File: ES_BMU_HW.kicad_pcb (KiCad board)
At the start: 2 copper layers, 100 x 100 mm, 105 parts, among them IC1 ADBMS6821CCSZ, J5 Conn_02x03_Top_Bottom, K1 FINDER-30.22, Q1 Si2366DS, Q2 Si2366DS, Q3 Si2366DS, Q4 2N7002, Q5 SQ2337CES, Q6 2N7002, SW3 SW_Nidec_CAS-120A1, T1 74941301, U1 TPS542025, U12 LM393, U13 74HC32, U15 SN65HVD235, U17 74AUP1G02, U18 74AUP1G08, U3 TLV1702, U4 TLV1702, U5 TLV1702, U6 STM32G474CETx, U7 TLV777, U8 TLV1704, U9 74HC04, Y1 16 MHz

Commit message: Canvi de microcontrolador Control dels relés de potència actualitzat Leds afegits per a visualitzar l'estat del fusible
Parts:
- removed C18, C19: 22p, Capacitor_SMD:C_1206_3216Metric
- removed K1: FINDER-30.22, Relay_THT:Relay_DPDT_Finder_30.22
- removed R1, R12, R14, R28, R7: 10K, Resistor_SMD:R_1206_3216Metric
- removed R13, R17, R22, R29, R5: 100K, Resistor_SMD:R_1206_3216Metric
- removed TP1, TP2, TP3, TP4: TestPoint, TestPoint:TestPoint_Pad_D1.0mm
- removed U13: 74HC32, Package_SO:TSSOP-14_4.4x5mm_P0.65mm
- removed U17: 74AUP1G02, Package_TO_SOT_SMD:Texas_R-PDSO-G5_DCK-5
- removed U18: 74AUP1G08, Package_TO_SOT_SMD:Texas_R-PDSO-G5_DCK-5
- removed U3, U4: TLV1702, Package_SO:VSSOP-8_3x3mm_P0.65mm
- removed U6: STM32G474CETx, Package_QFP:LQFP-48_7x7mm_P0.5mm
- removed U8: TLV1704, Package_SO:TSSOP-14_4.4x5mm_P0.65mm
- removed Y1: 16 MHz, Crystal_SMD_Wurth:Y_Wurth_WE-XTAL_Quartz-CFPX-180
- added C12: 10u, Capacitor_SMD:C_0603_1608Metric, F.Cu at (42.1, 61.0)
- added C16: 22p, Capacitor_SMD:C_1206_3216Metric, F.Cu at (66.2, 91.0)
- added C26: 22p, Capacitor_SMD:C_1206_3216Metric, F.Cu at (66.2, 94.4)
- added C27: 100n, Capacitor_SMD:C_0603_1608Metric, F.Cu at (42.1, 71.0)
- added D10: SMAJ30A, Diode_SMD:D_SMA, F.Cu at (23.1, 80.2)
- added D11: SMBJ3V3, Diode_SMD:D_SMB, F.Cu at (23.3, 89.8)
- added D12: SMBJ3V3, Diode_SMD:D_SMB, F.Cu at (23.3, 95.3)
- added D13: SMAJ30A, Diode_SMD:D_SMA, F.Cu at (23.1, 84.7)
- added D14: AR1FJ, Diode_SMD:D_SMF, F.Cu at (44.1, 89.1)
- added D16: SMAJ30A, Diode_SMD:D_SMA, F.Cu at (31.2, 62.0)
- added D17: SMAJ30A, Diode_SMD:D_SMA, F.Cu at (31.2, 66.5)
- added D19: SMAJ30A, Diode_SMD:D_SMA, F.Cu at (31.2, 71.1)
- added D2: SMAJ30A, Diode_SMD:D_SMA, F.Cu at (23.1, 62.0)
- added D20: AR1FJ, Diode_SMD:D_SMF, F.Cu at (44.1, 92.4)
- added D21: SMAJ30A, Diode_SMD:D_SMA, F.Cu at (31.2, 75.6)
- added D22: AR1FJ, Diode_SMD:D_SMF, F.Cu at (44.1, 95.8)
- added D23: SMAJ30A, Diode_SMD:D_SMA, F.Cu at (53.0, 66.5)
- added D24: D_Schottky, Diode_SMD:D_SMA, F.Cu at (53.0, 71.1)
- added D25: SMAJ30A, Diode_SMD:D_SMA, F.Cu at (53.0, 75.6)
- added D26: D_Schottky, Diode_SMD:D_SMA, F.Cu at (53.0, 80.2)
- added D27: SMAJ30A, Diode_SMD:D_SMA, F.Cu at (53.0, 84.7)
- added D28: SMAJ30A, Diode_SMD:D_SMA, F.Cu at (31.2, 80.2)
- added D3: SMAJ30A, Diode_SMD:D_SMA, F.Cu at (23.1, 66.5)
- added F2: Fuse, Fuse:Fuse_1206_3216Metric_Pad1.42x1.75mm_HandSolder, F.Cu at (38.2, 89.1)
- added F5: Fuse, Fuse:Fuse_1206_3216Metric_Pad1.42x1.75mm_HandSolder, F.Cu at (38.2, 92.4)
- added F6: Fuse, Fuse:Fuse_1206_3216Metric_Pad1.42x1.75mm_HandSolder, F.Cu at (38.2, 95.7)
- added Q7: SQ2362CES, Package_TO_SOT_SMD:SOT-23, F.Cu at (37.7, 71.4)
- added Q8: SQ2362CES, Package_TO_SOT_SMD:SOT-23, F.Cu at (37.7, 76.0)
- added R52: 100k, Resistor_SMD:R_0201_0603Metric_Pad0.64x0.40mm_HandSolder, F.Cu at (64.1, 77.9)
- added R53: 100k, Resistor_SMD:R_0201_0603Metric_Pad0.64x0.40mm_HandSolder, F.Cu at (64.1, 79.6)
- added U10: STM32G431RBTx, Package_QFP:LQFP-64_10x10mm_P0.5mm, F.Cu at (56.2, 96.6)
- added U11: LM393, Package_SO:TSSOP-8_4.4x3mm_P0.65mm, F.Cu at (61.4, 66.6)
- added U2: LM393, Package_SO:TSSOP-8_4.4x3mm_P0.65mm, F.Cu at (39.6, 80.5)
- added Y2: 16 MHz, Crystal_SMD_Wurth:Y_Wurth_WE-XTAL_Quartz-CFPX-180, F.Cu at (65.7, 98.7)
- C10, C15: value 15pF -> 100n; footprint Capacitor_SMD:C_1206_3216Metric -> Capacitor_SMD:C_0603_1608Metric
- C11: value 100nF -> 100n; footprint Capacitor_SMD:C_1206_3216Metric -> Capacitor_SMD:C_0603_1608Metric
- C13, C14: value 100nF -> 10u; footprint Capacitor_SMD:C_1206_3216Metric -> Capacitor_SMD:C_0603_1608Metric
- C9: value 10uF -> 100n; footprint Capacitor_SMD:C_1206_3216Metric -> Capacitor_SMD:C_0603_1608Metric
- D1: value SMBJ26A -> SMBJ30A
- D6: value SMBJ3V3 -> SMAJ30A; footprint Diode_SMD:D_SMB -> Diode_SMD:D_SMA
- D7: value SMBJ3V3 -> D_Schottky; footprint Diode_SMD:D_SMB -> Diode_SMD:D_SMA
- D9: value 1N4148W -> D_Schottky; footprint Diode_SMD:D_SOD-123 -> Diode_SMD:D_SMA
- Q1, Q2, Q3: value Si2366DS -> SQ2362CES
- Q4, Q6: value 2N7002 -> SQ2362CES
- Q5: value SQ2337CES -> SQ2362CES
- R10: value 10K -> 2k2; footprint Resistor_SMD:R_1206_3216Metric -> Resistor_SMD:R_0201_0603Metric_Pad0.64x0.40mm_HandSolder
- R11: value 100K -> 2k2; footprint Resistor_SMD:R_1206_3216Metric -> Resistor_SMD:R_0201_0603Metric_Pad0.64x0.40mm_HandSolder
- R15, R8: value 10K -> 470k; footprint Resistor_SMD:R_1206_3216Metric -> Resistor_SMD:R_0201_0603Metric_Pad0.64x0.40mm_HandSolder
- R16, R6, R9: value 10K -> 100k; footprint Resistor_SMD:R_1206_3216Metric -> Resistor_SMD:R_0201_0603Metric_Pad0.64x0.40mm_HandSolder
- R18, R20, R21, R23, R24: value 10K -> 10k; footprint Resistor_SMD:R_1206_3216Metric -> Resistor_SMD:R_0201_0603Metric_Pad0.64x0.40mm_HandSolder
- R19, R2, R25: value 100K -> 10k; footprint Resistor_SMD:R_1206_3216Metric -> Resistor_SMD:R_0201_0603Metric_Pad0.64x0.40mm_HandSolder
- R26, R27, R3, R4: value 100K -> 100k; footprint Resistor_SMD:R_1206_3216Metric -> Resistor_SMD:R_0201_0603Metric_Pad0.64x0.40mm_HandSolder
- R30: value 39k -> 100k; footprint Resistor_SMD:R_1206_3216Metric -> Resistor_SMD:R_0201_0603Metric_Pad0.64x0.40mm_HandSolder
- R31: value 68k -> 47k; footprint Resistor_SMD:R_1206_3216Metric -> Resistor_SMD:R_0201_0603Metric_Pad0.64x0.40mm_HandSolder
- R32: value 100k -> 47k; footprint Resistor_SMD:R_1206_3216Metric -> Resistor_SMD:R_0201_0603Metric_Pad0.64x0.40mm_HandSolder
- R33, R37, R38, R39, R42, R45, R47: footprint Resistor_SMD:R_1206_3216Metric -> Resistor_SMD:R_0201_0603Metric_Pad0.64x0.40mm_HandSolder
- R34: value 10 -> 47k; footprint Resistor_SMD:R_1206_3216Metric -> Resistor_SMD:R_0201_0603Metric_Pad0.64x0.40mm_HandSolder
- R35, R46: value 100k -> 470k; footprint Resistor_SMD:R_1206_3216Metric -> Resistor_SMD:R_0201_0603Metric_Pad0.64x0.40mm_HandSolder
- R36: value 150 -> 470k; footprint Resistor_SMD:R_1206_3216Metric -> Resistor_SMD:R_0201_0603Metric_Pad0.64x0.40mm_HandSolder
- U5: value TLV1702 -> LM393; footprint Package_SO:VSSOP-8_3x3mm_P0.65mm -> Package_SO:TSSOP-8_4.4x3mm_P0.65mm
- U9: value 74HC04 -> LM393; footprint Package_SO:TSSOP-14_4.4x5mm_P0.65mm -> Package_SO:TSSOP-8_4.4x3mm_P0.65mm
- moved U5 135.1 mm to (39.6, 85.1)
- moved R10 131.7 mm to (20.4, 101.0)
- moved Q1 126.9 mm to (37.7, 62.1)
- moved R11 108.3 mm to (20.4, 102.7)
- moved R16 108.1 mm to (45.6, 71.1)
- moved R15 108.1 mm to (45.6, 69.3)
- moved R8 102.6 mm to (45.6, 65.8)
- moved R9 102.5 mm to (45.6, 67.6)
- moved D7 102.1 mm to (23.1, 75.6)
- moved D6 102.0 mm to (23.1, 71.1)
- moved R18 101.6 mm to (58.5, 74.4)
- moved R20 101.2 mm to (58.5, 77.9)
- moved R21 101.1 mm to (58.5, 79.6)
- moved R6 97.2 mm to (45.6, 64.1)
- moved Q2 97.0 mm to (68.0, 75.9)
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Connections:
- net /SDCreset/BMSerror renamed /SDCreset/ControlAIR-
- net /stm32/SWCLK renamed /stm32/SWCLk
- C10 pad 1: /SDCreset/BMSerrorTime -> Net-(U11A-+)
- C11 pad 1: +24V -> Net-(U12A-+)
- C13 pad 1: +3.3V -> /GPIO/AuxAIR-
- C14 pad 1: +3.3V -> /GPIO/AuxAIR+
- C15 pad 1: Reset button conditioned -> Net-(U2A-+)
- C9 pad 1: Net-(U12A--) -> Net-(U9A-+)
- D5 pad 1: /GPIO/AuxAIRpre -> Net-(D5-A1)
- D6 pad 1: /GPIO/AuxAIR- -> Net-(D6-A1)
- D7 pad 1: /GPIO/AuxAIR+ -> Net-(D6-A1)
- D7 pad 2: GND -> /GPIO/ActiveButton
- D8 pad 1: Net-(D8-K) -> Net-(D16-A1)
- D8 pad 2: /GPIO/SDCend -> SDC
- D9 pad 1: SUPPLY -> /SDCreset/AIRpreCoil-
- IC1 pad 1: unconnected-(IC1-MSTR-Pad1) -> +3.3V
- IC1 pad 10: unconnected-(IC1-IM-Pad10) -> /stm32/IMA
- IC1 pad 11: unconnected-(IC1-IP-Pad11) -> /stm32/IPA
- IC1 pad 12: unconnected-(IC1-VDD-Pad12) -> +3.3V
- IC1 pad 13: unconnected-(IC1-VP-Pad13) -> +3.3V
- IC1 pad 17: unconnected-(IC1-NIC_1-Pad17) -> GND
- IC1 pad 18: unconnected-(IC1-NIC_2-Pad18) -> GND
- IC1 pad 19: unconnected-(IC1-NIC_3-Pad19) -> GND
- IC1 pad 2: unconnected-(IC1-PICO-Pad2) -> /stm32/SPI_MISO
- IC1 pad 20: unconnected-(IC1-NIC_4-Pad20) -> GND
- IC1 pad 21: unconnected-(IC1-NIC_5-Pad21) -> GND
- IC1 pad 22: unconnected-(IC1-NIC_6-Pad22) -> GND
- IC1 pad 23: unconnected-(IC1-NIC_7-Pad23) -> GND
- IC1 pad 24: unconnected-(IC1-NIC_8-Pad24) -> GND
- IC1 pad 25: unconnected-(IC1-NIC_9-Pad25) -> GND
- IC1 pad 26: unconnected-(IC1-NIC_10-Pad26) -> GND
- IC1 pad 27: unconnected-(IC1-NIC_11-Pad27) -> GND
- IC1 pad 28: unconnected-(IC1-NIC_12-Pad28) -> GND
- IC1 pad 29: unconnected-(IC1-NIC_13-Pad29) -> GND
- IC1 pad 3: unconnected-(IC1-POCI-Pad3) -> /stm32/SPI_MOSI
- IC1 pad 30: unconnected-(IC1-NIC_14-Pad30) -> GND
- IC1 pad 31: unconnected-(IC1-NIC_15-Pad31) -> GND
- IC1 pad 32: unconnected-(IC1-NIC_16-Pad32) -> GND
- IC1 pad 33: unconnected-(IC1-EP-Pad33) -> GND
- IC1 pad 4: unconnected-(IC1-SCK-Pad4) -> /stm32/SPI_SCk
- IC1 pad 6: unconnected-(IC1-VDDS-Pad6) -> +3.3V
- IC1 pad 9: unconnected-(IC1-GND-Pad9) -> GND
- Q1 pad 1: /GPIO/ControlAIR+ -> /GPIO/ControlAIR-
- Q1 pad 3: /GPIO/AIR+Coil- -> /GPIO/AIR-Coil-
- Q2 pad 1: /GPIO/ControlAIR- -> /SDCreset/ControlAIRpre
- Q2 pad 3: /GPIO/AIR-Coil- -> /SDCreset/AIRpreCoil-
- Q4 pad 3: Net-(Q4-D) -> /SDCreset/AIR-Coil-
- Q5 pad 1: Net-(Q5-G) -> /SDCreset/ControlAIR+
- Q5 pad 2: +3.3V -> GND
- Q5 pad 3: Net-(Q5-D) -> /SDCreset/AIR+Coil-
- Q6 pad 1: Net-(Q6-G) -> /GPIO/ControlAIR+
- Q6 pad 3: Net-(D9-A) -> /GPIO/AIR+Coil-
- R10 pad 1: Net-(U4B--) -> VBAT
- R10 pad 2: 24V -> Net-(D29-A)
- R11 pad 1: Net-(U5A--) -> +24V
- R11 pad 2: +5V -> Net-(D30-A)
- R15 pad 1: /GPIO/3.3V -> Net-(U5A-+)
- R15 pad 2: /GPIO/WireCheckAIR+3.3 -> GND
- R16 pad 1: Net-(U5B--) -> Net-(U5A-+)
- R16 pad 2: 24V -> Net-(D16-A1)
- R18 pad 1: Net-(U5B--) -> /SDCreset/3.3V
- R18 pad 2: GND -> /SDCreset/WireCheckAIRpre24
- R19 pad 1: Net-(D8-K) -> /SDCreset/3.3V
- R19 pad 2: GND -> /SDCreset/WireCheckAIRpre3.3
- R2 pad 1: /GPIO/AuxAIR- -> /GPIO/3.3V
- R2 pad 2: GND -> /GPIO/ActiveButtonState
- R20 pad 1: /GPIO/3.3V -> /SDCreset/3.3V
- R20 pad 2: /GPIO/AIRpreCoil- -> /SDCreset/WireCheckAIR-24
- R21 pad 1: /GPIO/3.3V -> /SDCreset/3.3V
- R21 pad 2: /GPIO/AIRpreCoil- -> /SDCreset/WireCheckAIR-3.3
- R23 pad 1: /GPIO/3.3V -> /SDCreset/3.3V
- R23 pad 2: /GPIO/ActivButton -> /SDCreset/WireCheckAIR+24
- R25 pad 1: Net-(U4A--) -> /SDCreset/3.3V
- R25 pad 2: +5V -> /SDCreset/WireCheckAIR+3.3
- R26 pad 1: Net-(U4A--) -> Net-(U9A--)
- R26 pad 2: GND -> +5V
- R27 pad 1: /GPIO/RawActivButton -> Net-(U11A--)
- R27 pad 2: GND -> +5V
- R30 pad 1: +3.3V -> Net-(U12A--)
- R30 pad 2: /SDCreset/Plausibity error threshold -> +5V
- R31 pad 1: /SDCreset/Plausibity error threshold -> Net-(U9A--)
- R32 pad 1: +3.3V -> Net-(U11A--)
- R32 pad 2: Net-(Q4-D) -> GND
- R34 pad 1: Net-(Q4-D) -> Net-(U12A--)
- R34 pad 2: Net-(U12A--) -> GND
- R35 pad 1: +3.3V -> Net-(U9A-+)
- R35 pad 2: /SDCreset/BMSerrorTime -> GND
- R36 pad 1: Net-(Q5-D) -> Net-(U11A-+)
- R36 pad 2: BMS error dash Indicator -> GND
- R4 pad 1: Net-(U3A--) -> /GPIO/AuxAIR-
- R4 pad 2: +5V -> GND
- R46 pad 1: Reset button -> Net-(U12A-+)
- R46 pad 2: +5V -> GND
- R47 pad 1: Reset button conditioned -> Net-(U9A-+)
- R47 pad 2: +3.3V -> /SDCreset/AIRpreCoil-
- R6 pad 1: /GPIO/3.3V -> /GPIO/AuxAIR+
- R6 pad 2: /GPIO/WireCheckAIRpre24 -> GND
- R8 pad 1: /GPIO/3.3V -> Net-(U2A-+)
- R8 pad 2: /GPIO/WireCheckAIR-24 -> GND
- R9 pad 1: /GPIO/3.3V -> Net-(U2A-+)
- R9 pad 2: /GPIO/WireCheckAIR-3.3 -> Net-(D6-A1)
- T1 pad 1: unconnected-(T1-Pad1) -> /stm32/IPA
- T1 pad 3: unconnected-(T1-Pad3) -> /stm32/IMA
- U12 pad 1: /SDCreset/BMSerrorTime -> /SDCreset/WireCheckAIR+3.3
- U12 pad 3: /SDCreset/Plausibity error threshold -> Net-(U12A-+)
- U12 pad 4: GND -> (no net)
- U12 pad 5: +3.3V -> Net-(U12A-+)
- U12 pad 6: Reset button -> +5V
- U12 pad 7: Reset button conditioned -> /SDCreset/WireCheckAIR+24
- U12 pad 8: +24V -> (no net)
- U5 pad 1: /GPIO/WireCheckAIR+3.3 -> /GPIO/SDCendState
- U5 pad 2: Net-(U5A--) -> +5V
- U5 pad 3: /GPIO/WireCheckAIR+ -> Net-(U5A-+)
- U5 pad 5: /GPIO/WireCheckAIR+ -> (no net)
- U5 pad 6: Net-(U5B--) -> (no net)
- U5 pad 7: /GPIO/WireCheckAIR+24 -> (no net)
- U9 pad 1: /SDCreset/BMSset -> /SDCreset/WireCheckAIRpre3.3
- U9 pad 2: Net-(U13-Pad5) -> Net-(U9A--)
- U9 pad 3: Net-(U17-Pad4) -> Net-(U9A-+)
- U9 pad 4: Net-(Q5-G) -> (no net)
- U9 pad 5: /SDCreset/BMSset -> Net-(U9A-+)
- U9 pad 6: Net-(U13-Pad10) -> +5V
- U9 pad 7: GND -> /SDCreset/WireCheckAIRpre24

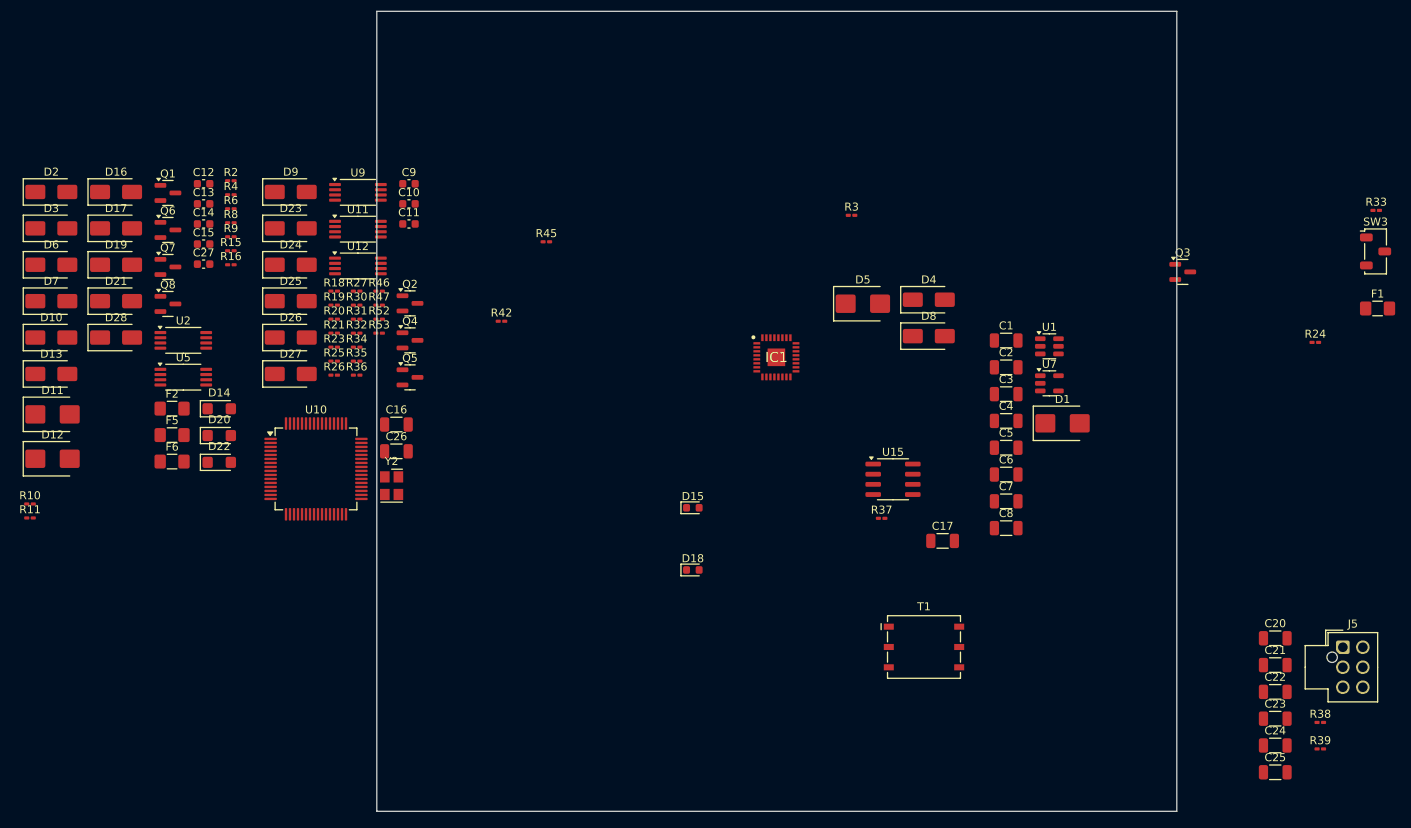
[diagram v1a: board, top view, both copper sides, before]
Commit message: - Reorganització dels components al fitxer de stm32 - S'ha afegit el ADC ADS1113IDGS per la lectura del sensor Hall - Modificació del tranceptor CAN al SN65HVD234 - Eliminació del pin SWO - S'ha afegit el pin de enable per a cada tranceptor
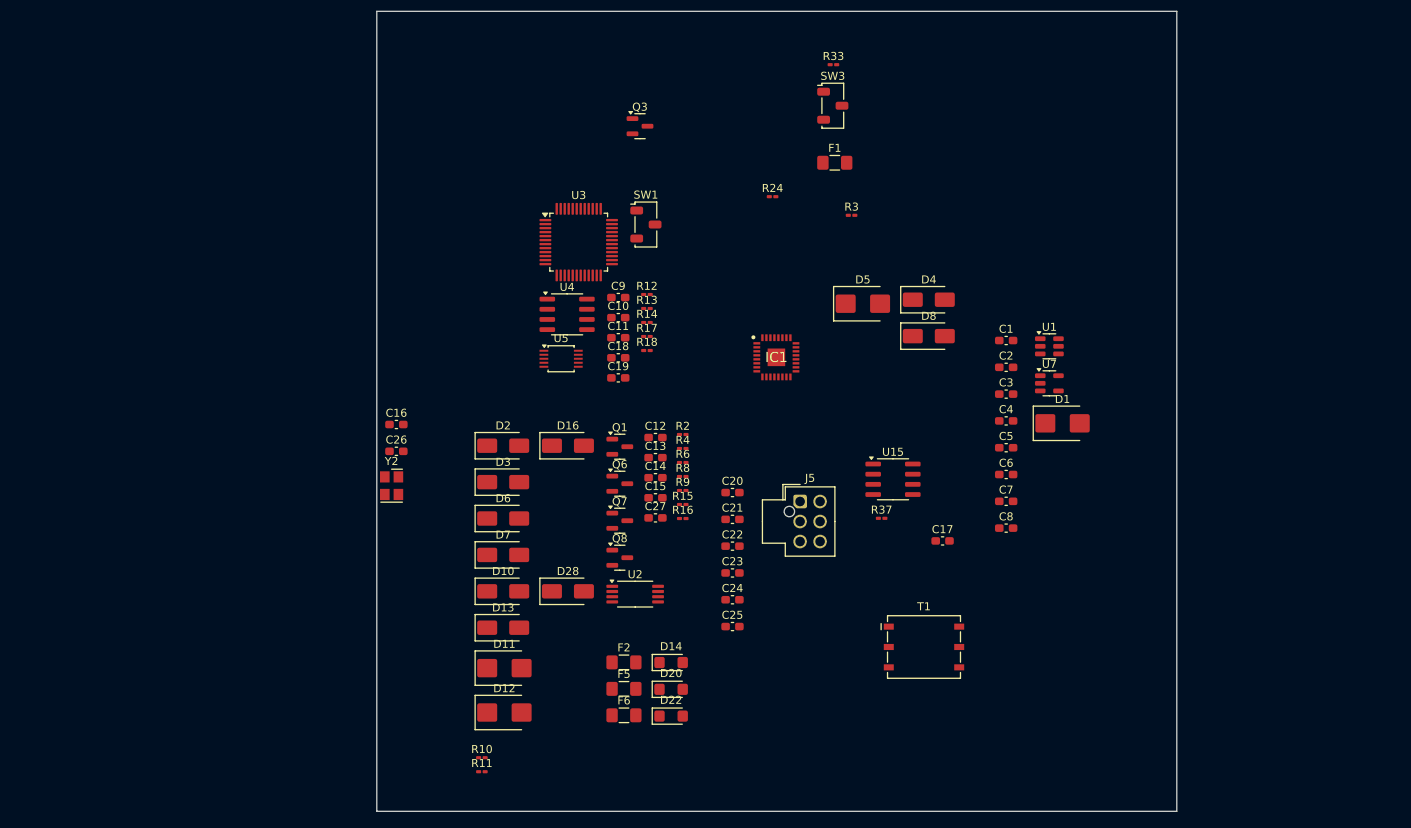
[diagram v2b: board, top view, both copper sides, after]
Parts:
- removed D15, D18: LED, LED_SMD:LED_0603_1608Metric
- removed D17, D19, D21, D23, D25, D27: SMAJ30A, Diode_SMD:D_SMA
- removed D24, D26, D9: D_Schottky, Diode_SMD:D_SMA
- removed Q2, Q4, Q5: SQ2362CES, Package_TO_SOT_SMD:SOT-23
- removed R19, R20, R21, R23, R25: 10k, Resistor_SMD:R_0201_0603Metric_Pad0.64x0.40mm_HandSolder
- removed R26, R27, R30, R38, R39, R47, R52, R53: 100k, Resistor_SMD:R_0201_0603Metric_Pad0.64x0.40mm_HandSolder
- removed R31, R32, R34: 47k, Resistor_SMD:R_0201_0603Metric_Pad0.64x0.40mm_HandSolder
- removed R35, R36, R46: 470k, Resistor_SMD:R_0201_0603Metric_Pad0.64x0.40mm_HandSolder
- removed R42: 150, Resistor_SMD:R_0201_0603Metric_Pad0.64x0.40mm_HandSolder
- removed R45: 50, Resistor_SMD:R_0201_0603Metric_Pad0.64x0.40mm_HandSolder
- removed U10: STM32G431RBTx, Package_QFP:LQFP-64_10x10mm_P0.5mm
- removed U11, U12, U9: LM393, Package_SO:TSSOP-8_4.4x3mm_P0.65mm
- added C18: 1u, Capacitor_SMD:C_0603_1608Metric_Pad1.08x0.95mm_HandSolder, F.Cu at (94.0, 82.7)
- added C19: 15p, Capacitor_SMD:C_0603_1608Metric_Pad1.08x0.95mm_HandSolder, F.Cu at (94.0, 85.2)
- added R12: 100k, Resistor_SMD:R_0201_0603Metric_Pad0.64x0.40mm_HandSolder, F.Cu at (97.6, 74.8)
- added R13: 120, Resistor_SMD:R_0201_0603Metric_Pad0.64x0.40mm_HandSolder, F.Cu at (97.6, 76.5)
- added R14: 10k, Resistor_SMD:R_0201_0603Metric_Pad0.64x0.40mm_HandSolder, F.Cu at (97.6, 78.3)
- added R17: 100k, Resistor_SMD:R_0201_0603Metric_Pad0.64x0.40mm_HandSolder, F.Cu at (97.6, 80.0)
- added SW1: SW_Nidec_CAS-120A1, Button_Switch_SMD:Nidec_Copal_CAS-120A, F.Cu at (97.4, 66.0)
- added U3: STM32G474CETx, Package_QFP:LQFP-48_7x7mm_P0.5mm, F.Cu at (89.0, 68.2)
- added U4: SN65HVD234, Package_SO:SOIC-8_3.9x4.9mm_P1.27mm, F.Cu at (87.6, 77.3)
- C1, C16, C17, C2, C20, C21, C22, C23, C24, C25, C26, C3, C4, C5, C6, C7, C8: footprint Capacitor_SMD:C_1206_3216Metric -> Capacitor_SMD:C_0603_1608Metric_Pad1.08x0.95mm_HandSolder
- C10, C11, C12, C13, C14, C15, C27, C9: footprint Capacitor_SMD:C_0603_1608Metric -> Capacitor_SMD:C_0603_1608Metric_Pad1.08x0.95mm_HandSolder
- R18: value 10k -> 100k
- U15: value SN65HVD235 -> SN65HVD234
- U5: value LM393 -> ADS1113IDGS; footprint Package_SO:TSSOP-8_4.4x3mm_P0.65mm -> Package_SO:TSSOP-10_3x3mm_P0.5mm
- moved F1 70.2 mm to (121.0, 58.3)
- moved R24 70.2 mm to (113.3, 62.6)
- moved SW3 70.2 mm to (120.8, 51.2)
- moved J5 70.2 mm to (116.7, 100.7)
- moved R33 70.2 mm to (120.9, 46.1)
- moved C20 70.2 mm to (108.3, 99.6)
- moved C21 70.2 mm to (108.3, 102.9)
- moved C22 70.2 mm to (108.3, 106.3)
- moved C23 70.2 mm to (108.3, 109.6)
- moved C24 70.2 mm to (108.3, 113.0)
- moved C25 70.2 mm to (108.3, 116.3)
- moved Q3 70.2 mm to (96.7, 53.8)
- moved C12 64.8 mm to (98.6, 92.7)
- moved C13 64.8 mm to (98.6, 95.2)
- moved C14 64.8 mm to (98.6, 97.7)
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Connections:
- net /stm32/CANH renamed /stm32/CAN1H
- net /stm32/CANL renamed /stm32/CAN1L
- net /stm32/FDCAN_RX renamed /stm32/FDCAN1_RX
- C10 pad 1: Net-(U11A-+) -> +3.3V
- C11 pad 1: Net-(U12A-+) -> +3.3V
- C27 pad 1: Net-(U5A-+) -> Net-(U2B-+)
- C9 pad 1: Net-(U9A-+) -> +3.3V
- D14 pad 2: Net-(D14-A) -> /GPIO/AIRpreCoil-
- D20 pad 2: Net-(D19-A2) -> /GPIO/AIR-Coil-
- D22 pad 2: Net-(D21-A2) -> /GPIO/AIR+Coil-
- D8 pad 2: SDC -> /GPIO/SDCinput
- IC1 pad 14: unconnected-(IC1-PHAPOL-Pad14) -> +3.3V
- IC1 pad 15: unconnected-(IC1-RTO-Pad15) -> Net-(IC1-RTO)
- IC1 pad 16: unconnected-(IC1-XCVRMD-Pad16) -> GND
- IC1 pad 2: /stm32/SPI_MISO -> /stm32/SPI1_MISO
- IC1 pad 3: /stm32/SPI_MOSI -> /stm32/SPI1_MOSI
- IC1 pad 4: /stm32/SPI_SCk -> /stm32/SPI1_SCK
- IC1 pad 5: unconnected-(IC1-~{CS}-Pad5) -> /stm32/SPI1_CS
- IC1 pad 7: unconnected-(IC1-INTR-Pad7) -> /stm32/SPI1_INTR
- IC1 pad 8: unconnected-(IC1-WAKE-Pad8) -> /stm32/SPI1_WAKE
- J5 pad 4: /stm32/SWCLk -> /stm32/SWCLK
- J5 pad 6: SWO -> unconnected-(J5-Pin_6-Pad6)
- R15 pad 1: Net-(U5A-+) -> Net-(U2B-+)
- R16 pad 1: Net-(U5A-+) -> Net-(U2B-+)
- R18 pad 1: /SDCreset/3.3V -> /stm32/SWCLK
- R18 pad 2: /SDCreset/WireCheckAIRpre24 -> GND
- T1 pad 4: unconnected-(T1-Pad4) -> /stm32/IMA_EXT
- T1 pad 6: unconnected-(T1-Pad6) -> /stm32/IPA_EXT
- U15 pad 1: /stm32/FDCAN_TX -> /stm32/FDCAN1_TX
- U15 pad 5: GND -> /stm32/FDCAN1_EN
- U2 pad 4: (no net) -> GND
- U2 pad 5: (no net) -> Net-(U2B-+)
- U2 pad 6: (no net) -> +5V
- U2 pad 7: (no net) -> /GPIO/SDCendState
- U2 pad 8: (no net) -> +24V
- U5 pad 1: /GPIO/SDCendState -> GND
- U5 pad 2: +5V -> unconnected-(U5-Pad2)
- U5 pad 3: Net-(U5A-+) -> GND
- U5 pad 4: (no net) -> /stm32/HallVout
- U5 pad 5: (no net) -> unconnected-(U5-AIN1-Pad5)
- U5 pad 6: (no net) -> unconnected-(U5-Pad6)
- U5 pad 7: (no net) -> unconnected-(U5-Pad7)
- U5 pad 8: (no net) -> +3.3V
